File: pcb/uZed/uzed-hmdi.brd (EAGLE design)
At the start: 77.5 x 58.1 mm, 6 parts, among them U11 PCA9306

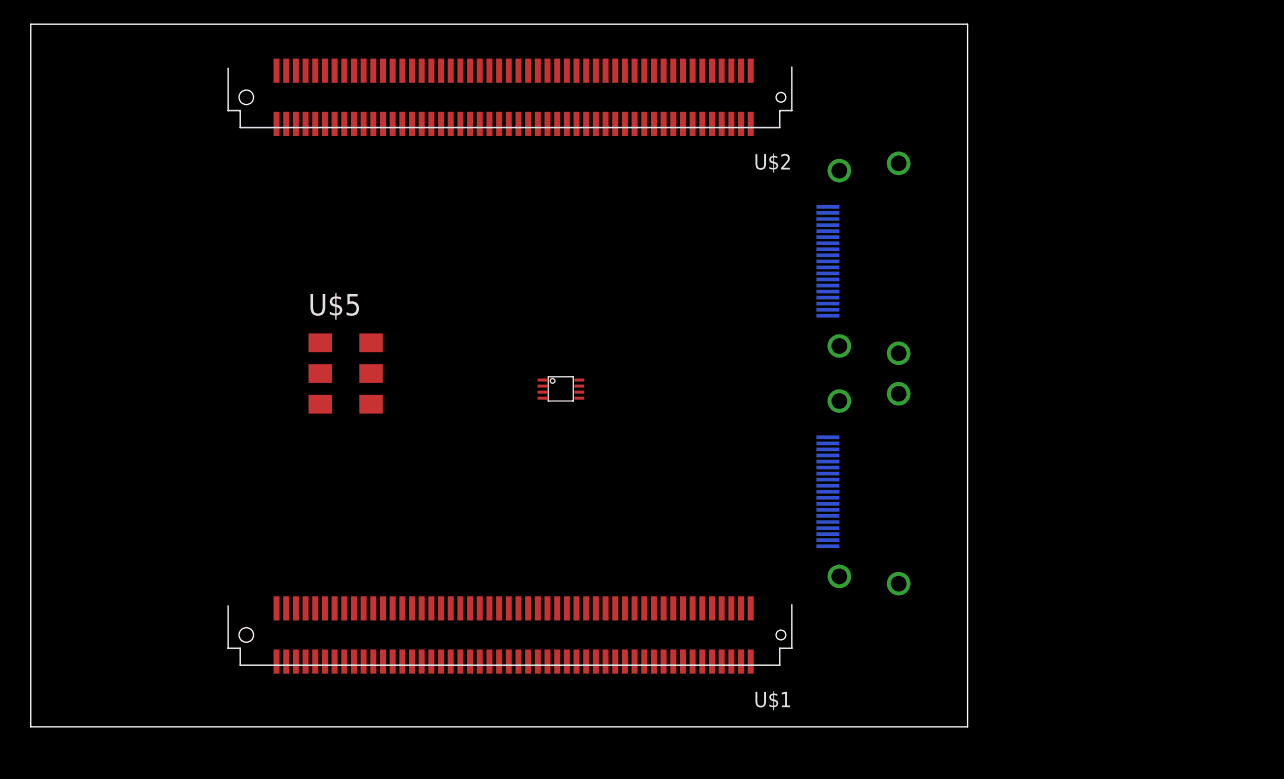
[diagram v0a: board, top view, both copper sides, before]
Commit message: hdmi connections copied in from scarab hardware board
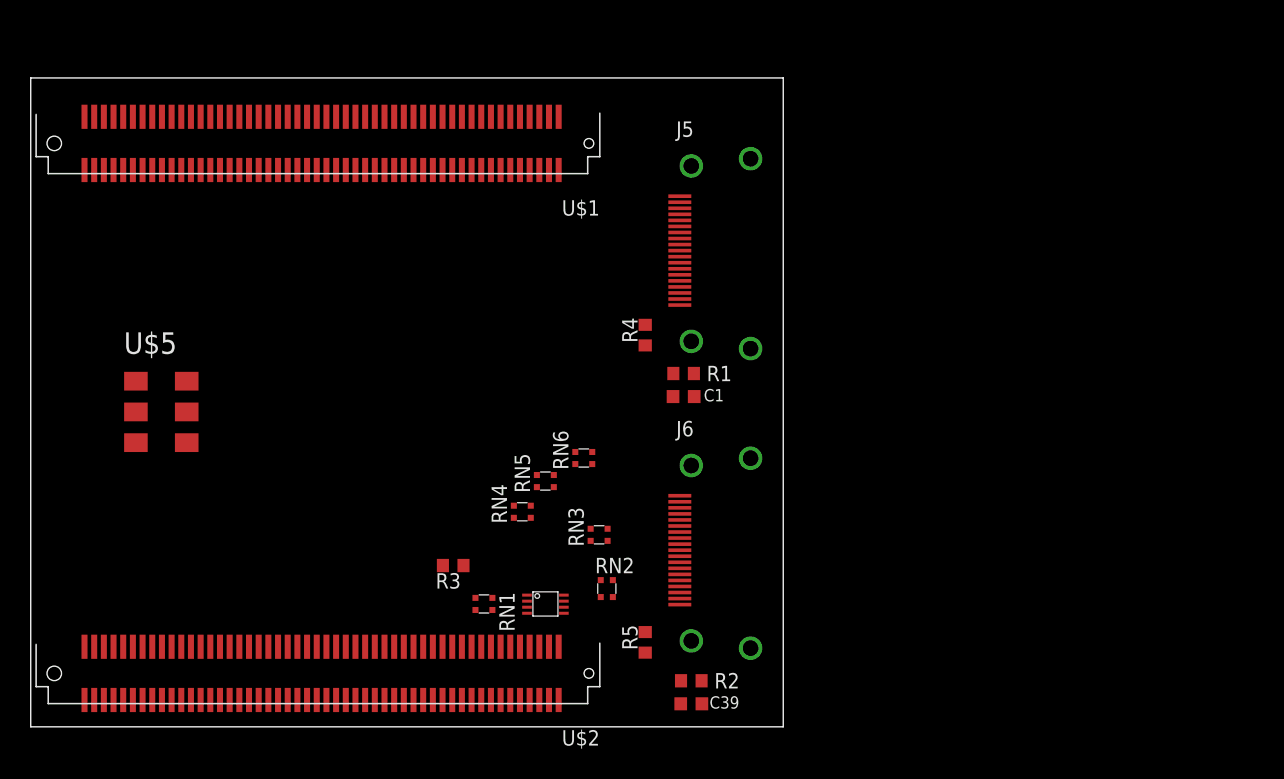
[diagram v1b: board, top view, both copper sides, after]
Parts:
- removed U$3, U$4: HDMI-A, new-connectors:HDMI_A
- removed U11: PCA9306, saanlima:PSOP-8
- added C1, C39: .1uF, rcl:C0603K
- added J5, J6: HDMI-TYPE-A-RECEPTICALFCI10029449, saanlima:FCI-HDMI-TYPE-A-RECEPT
- added PCA9306: PCA9306, saanlima:PSOP-8
- added R1, R2: 100K, rcl:R0603
- added R3: 0, rcl:R0603
- added R4, R5: 10K, rcl:R0603
- added RN1, RN2: 2k, resistor-dil:EXB34V
- added RN3, RN4, RN5, RN6: 51, resistor-dil:EXB34V
- moved U$2 50.2 mm to (4.45, 7.62)
- moved U$1 43.6 mm to (4.45, 51.4)
- moved U$5 15.6 mm to (10.8, 26.0)
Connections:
- new net 3V3: PCA9306.2, R3.2, RN1.3, RN1.4
- new net GND: C1.2, C39.2, J5.11, J5.14, J5.17, J5.2, J5.5, J5.8, J6.11, J6.14, J6.17, J6.2, J6.5, J6.8, PCA9306.1, R1.1, R2.1, R4.1
- new net N$1: C1.1, J5.SH1, J5.SH2, J5.SH3, J5.SH4, R1.2
- new net N$10: J5.19, R4.2
- new net N$11: R3.1, RN3.3, RN3.4, RN4.3, RN4.4, RN5.3, RN5.4, RN6.3, RN6.4
- new net N$12: J6.19, R5.1
- new net N$13: J6.18, PCA9306.7, PCA9306.8, R5.2, RN2.3, RN2.4
- new net N$15: J6.16, PCA9306.5, RN2.2
- new net N$16: J6.15, PCA9306.6, RN2.1
- new net N$17: PCA9306.3, RN1.1
- new net N$18: PCA9306.4, RN1.2
- new net N$19: J5.1
- new net N$2: J6.1, RN6.2
- new net N$20: J5.3
- new net N$21: J5.4
- new net N$22: J5.6
- new net N$23: J5.7
- new net N$24: J5.9
- new net N$25: J5.10
- new net N$26: J5.12
- new net N$3: J6.3, RN6.1
- new net N$34: C39.1, J6.SH1, J6.SH2, J6.SH3, J6.SH4, R2.2
- new net N$4: J6.4, RN5.2
- new net N$5: J6.6, RN5.1
- new net N$6: J6.7, RN4.2
- new net N$7: J6.9, RN4.1
- new net N$8: J6.10, RN3.2
- new net N$9: J6.12, RN3.1
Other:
- board size 77.5 x 58.1 mm -> 62.2 x 53.6 mm

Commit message: hdmi added in from scarab board
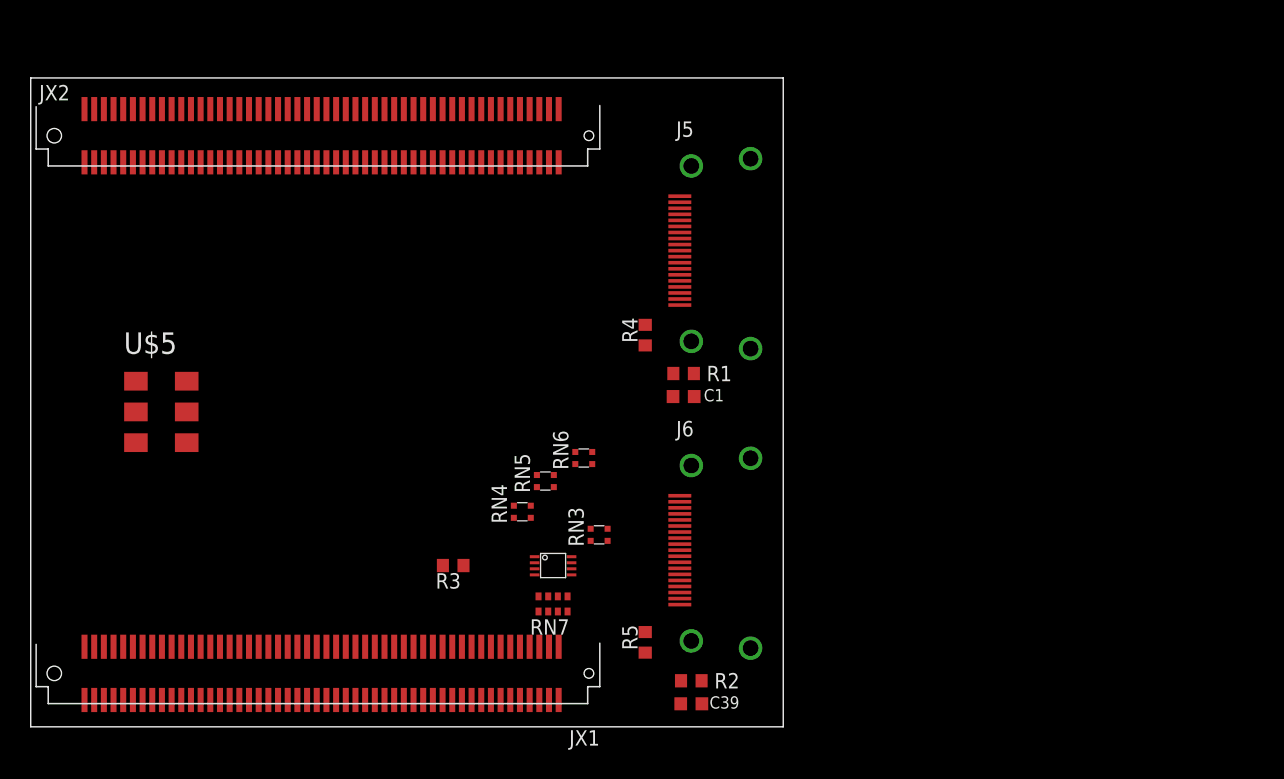
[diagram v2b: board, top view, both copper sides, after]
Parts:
- removed RN1, RN2: 2k, resistor-dil:EXB34V
- removed U$1: BERGSTAK-100POS, lupa300-components:BERG100POS
- added JX2: BERGSTAK-100POS, lupa300-components:BERG100POS
- added RN7: 2k, resistor-dil:0603-ARV
- moved PCA9306 3.24 mm to (43.2, 13.3)
- renumbered U$2 to JX1
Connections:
- net 3V3: now also RN7.1, RN7.2; no longer RN1.3, RN1.4
- net N$13: now also RN7.3, RN7.4; no longer RN2.3, RN2.4
- net N$15: now also RN7.6; no longer RN2.2
- net N$16: now also RN7.5; no longer RN2.1
- net N$17: now also RN7.7; no longer RN1.1
- net N$18: now also RN7.8; no longer RN1.2
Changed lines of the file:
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@@
 <dimension x1="0" y1="0" x2="62.21" y2="0" x3="31.105" y3="-5.08" textsize="1.778" layer="1"/>
 <dimension x1="0" y1="0" x2="0" y2="53.645" x3="-17.78" y3="26.8225" textsize="1.778" layer="1"/>
+<dimension x1="1.905" y1="4.445" x2="1.905" y2="48.895" x3="-9.525" y3="26.67" textsize="1.778" layer="1" unit="mil"/>
 </plain>
 <attributes>
@@
 </autorouter>
 <elements>
-<element name="U$1" library="lupa300-components" package="BERG100POS" value="BERGSTAK-100POS" x="4.445" y="51.435" smashed="yes" rot="R180">
-<attribute name="NAME" x="47.045" y="43.535" size="1.27" layer="25" rot="R180"/>
-</element>
-<element name="U$2" library="lupa300-components" package="BERG100POS" value="BERGSTAK-100POS" x="4.445" y="7.62" smashed="yes" rot="R180">
+<element name="JX2" library="lupa300-components" package="BERG100POS" value="BERGSTAK-100POS" x="4.445" y="52.07" smashed="yes" rot="R180">
+<attribute name="NAME" x="3.23" y="53.06" size="1.27" layer="25" rot="R180"/>
+</element>
+<element name="JX1" library="lupa300-components" package="BERG100POS" value="BERGSTAK-100POS" x="4.445" y="7.62" smashed="yes" rot="R180">
 <attribute name="NAME" x="47.045" y="-0.28" size="1.27" layer="25" rot="R180"/>
 </element>
@@
 <element name="R4" library="rcl" package="R0603" value="10K" x="50.8" y="32.385" rot="R90"/>
 <element name="R5" library="rcl" package="R0603" value="10K" x="50.8" y="6.985" rot="R90"/>
-<element name="PCA9306" library="saanlima" package="PSOP-8" value="PCA9306" x="42.545" y="10.16" rot="R270"/>
-<element name="RN1" library="resistor-dil" library_urn="urn:adsk.eagle:library:342" package="EXB34V" package3d_urn="urn:adsk.eagle:package:24930/1" value="2k" x="37.465" y="10.16" rot="R270">
-<attribute name="MF" value="" x="37.465" y="10.16" size="1.778" layer="27" rot="R270" display="off"/>
-<attribute name="MPN" value="" x="37.465" y="10.16" size="1.778" layer="27" rot="R270" display="off"/>
-<attribute name="OC_FARNELL" value="unknown" x="37.465" y="10.16" size="1.778" layer="27" rot="R270" display="off"/>
-<attribute name="OC_NEWARK" value="unknown" x="37.465" y="10.16" size="1.778" layer="27" rot="R270" display="off"/>
-</element>
-<element name="RN2" library="resistor-dil" library_urn="urn:adsk.eagle:library:342" package="EXB34V" package3d_urn="urn:adsk.eagle:package:24930/1" value="2k" x="47.625" y="11.43">
-<attribute name="MF" value="" x="47.625" y="11.43" size="1.778" layer="27" display="off"/>
-<attribute name="MPN" value="" x="47.625" y="11.43" size="1.778" layer="27" display="off"/>
-<attribute name="OC_FARNELL" value="unknown" x="47.625" y="11.43" size="1.778" layer="27" display="off"/>
-<attribute name="OC_NEWARK" value="unknown" x="47.625" y="11.43" size="1.778" layer="27" display="off"/>
+<element name="PCA9306" library="saanlima" package="PSOP-8" value="PCA9306" x="43.18" y="13.335" rot="R270"/>
+<element name="RN7" library="resistor-dil" package="0603-ARV" value="2k" x="43.18" y="10.16">
+<attribute name="MF" value="" x="43.18" y="10.16" size="1.778" layer="27" display="off"/>
+<attribute name="MPN" value="" x="43.18" y="10.16" size="1.778" layer="27" display="off"/>
+<attribute name="OC_FARNELL" value="unknown" x="43.18" y="10.16" size="1.778" layer="27" display="off"/>
+<attribute name="OC_NEWARK" value="unknown" x="43.18" y="10.16" size="1.778" layer="27" display="off"/>
 </element>
 </elements>
@@
 <wire x1="53.76" y1="3.81" x2="53.66" y2="11.105" width="0" layer="19" extent="1-1"/>
 <wire x1="53.735" y1="1.905" x2="53.76" y2="3.81" width="0" layer="19" extent="1-1"/>
-<wire x1="41.025" y1="10.89" x2="53.66" y2="11.105" width="0" layer="19" extent="1-1"/>
+<wire x1="41.66" y1="14.065" x2="53.66" y2="11.105" width="0" layer="19" extent="1-1"/>
 </signal>
 <signal name="N$34">
@@
 <contactref element="R3" pad="2"/>
 <contactref element="PCA9306" pad="2"/>
-<contactref element="RN1" pad="4"/>
-<contactref element="RN1" pad="3"/>
-<wire x1="38.165" y1="10.66" x2="41.025" y2="10.39" width="0" layer="19" extent="1-1"/>
-<wire x1="38.165" y1="9.66" x2="38.165" y2="10.66" width="0" layer="19" extent="1-1"/>
-<wire x1="34.075" y1="13.335" x2="38.165" y2="10.66" width="0" layer="19" extent="1-1"/>
+<contactref element="RN7" pad="2"/>
+<contactref element="RN7" pad="1"/>
+<wire x1="34.075" y1="13.335" x2="41.66" y2="13.565" width="0" layer="19" extent="1-1"/>
+<wire x1="42.78" y1="9.535" x2="34.075" y2="13.335" width="0" layer="19" extent="1-1"/>
+<wire x1="41.98" y1="9.535" x2="42.78" y2="9.535" width="0" layer="19" extent="1-1"/>
 </signal>
 <signal name="N$10">
@@
 <contactref element="PCA9306" pad="8"/>
 <contactref element="PCA9306" pad="7"/>
-<contactref element="RN2" pad="4"/>
-<contactref element="RN2" pad="3"/>
+<contactref element="RN7" pad="4"/>
+<contactref element="RN7" pad="3"/>
 <wire x1="50.8" y1="7.835" x2="53.66" y2="10.605" width="0" layer="19" extent="1-1"/>
-<wire x1="48.125" y1="12.13" x2="50.8" y2="7.835" width="0" layer="19" extent="1-1"/>
-<wire x1="47.125" y1="12.13" x2="48.125" y2="12.13" width="0" layer="19" extent="1-1"/>
-<wire x1="44.075" y1="10.89" x2="47.125" y2="12.13" width="0" layer="19" extent="1-1"/>
-<wire x1="44.075" y1="10.39" x2="44.075" y2="10.89" width="0" layer="19" extent="1-1"/>
+<wire x1="44.71" y1="13.565" x2="50.8" y2="7.835" width="0" layer="19" extent="1-1"/>
+<wire x1="44.71" y1="14.065" x2="44.71" y2="13.565" width="0" layer="19" extent="1-1"/>
+<wire x1="44.38" y1="9.535" x2="44.71" y2="14.065" width="0" layer="19" extent="1-1"/>
+<wire x1="43.58" y1="9.535" x2="44.38" y2="9.535" width="0" layer="19" extent="1-1"/>
 </signal>
 <signal name="N$15">
 <contactref element="J6" pad="16"/>
 <contactref element="PCA9306" pad="5"/>
-<contactref element="RN2" pad="2"/>
-<wire x1="48.125" y1="10.73" x2="53.66" y2="11.605" width="0" layer="19" extent="1-1"/>
-<wire x1="44.075" y1="9.39" x2="48.125" y2="10.73" width="0" layer="19" extent="1-1"/>
+<contactref element="RN7" pad="6"/>
+<wire x1="44.71" y1="12.565" x2="53.66" y2="11.605" width="0" layer="19" extent="1-1"/>
+<wire x1="43.58" y1="10.785" x2="44.71" y2="12.565" width="0" layer="19" extent="1-1"/>
 </signal>
 <signal name="N$16">
 <contactref element="J6" pad="15"/>
 <contactref element="PCA9306" pad="6"/>
-<contactref element="RN2" pad="1"/>
-<wire x1="47.125" y1="10.73" x2="53.66" y2="12.105" width="0" layer="19" extent="1-1"/>
-<wire x1="44.075" y1="9.89" x2="47.125" y2="10.73" width="0" layer="19" extent="1-1"/>
+<contactref element="RN7" pad="5"/>
+<wire x1="44.71" y1="13.065" x2="53.66" y2="12.105" width="0" layer="19" extent="1-1"/>
+<wire x1="44.38" y1="10.785" x2="44.71" y2="13.065" width="0" layer="19" extent="1-1"/>
 </signal>
 <signal name="N$17">
 <contactref element="PCA9306" pad="3"/>
-<contactref element="RN1" pad="1"/>
-<wire x1="36.765" y1="10.66" x2="41.025" y2="9.89" width="0" layer="19" extent="1-1"/>
+<contactref element="RN7" pad="7"/>
+<wire x1="42.78" y1="10.785" x2="41.66" y2="13.065" width="0" layer="19" extent="1-1"/>
 </signal>
 <signal name="N$18">
 <contactref element="PCA9306" pad="4"/>
-<contactref element="RN1" pad="2"/>
-<wire x1="36.765" y1="9.66" x2="41.025" y2="9.39" width="0" layer="19" extent="1-1"/>
+<contactref element="RN7" pad="8"/>
+<wire x1="41.98" y1="10.785" x2="41.66" y2="12.565" width="0" layer="19" extent="1-1"/>
 </signal>
 <signal name="N$19">

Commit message: more work on hdmi, layout with mounting holes complete, bergstak connectors aligned to be to carrier board spec
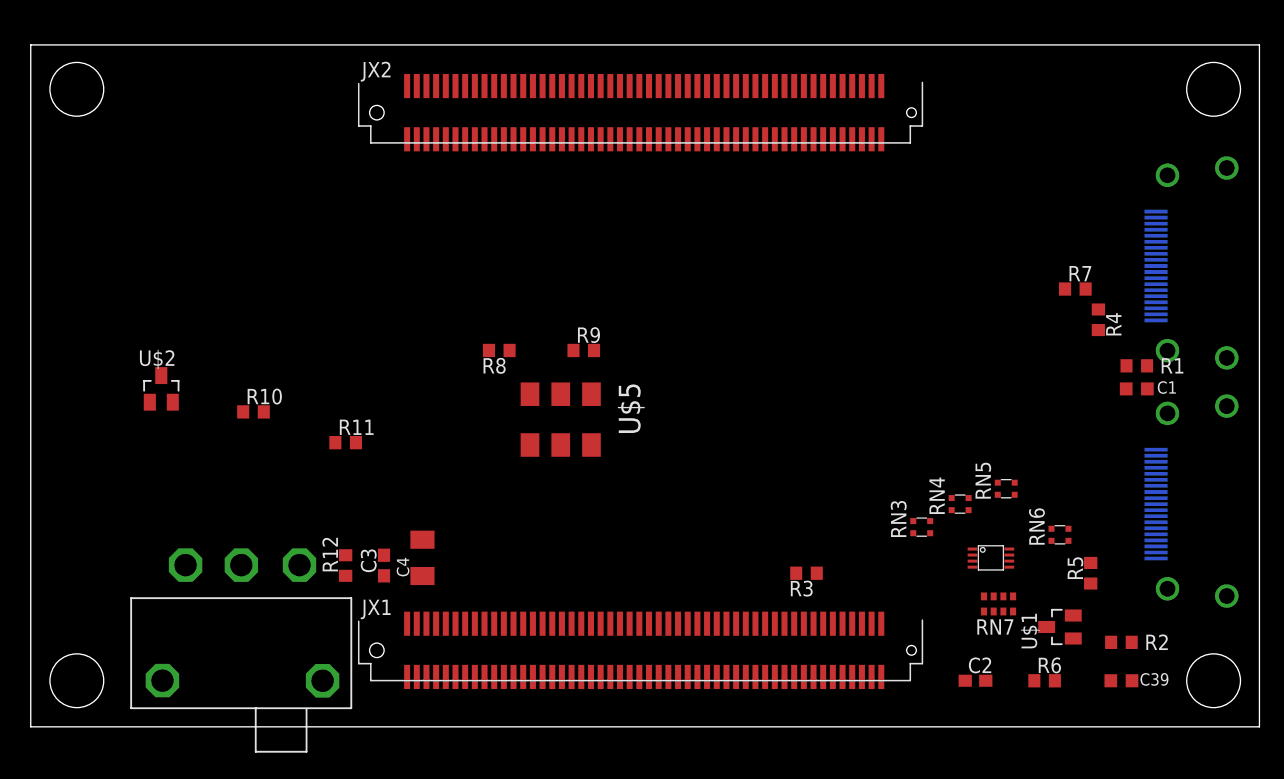
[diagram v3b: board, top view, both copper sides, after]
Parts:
- added C2: 100nF, rcl:C0603
- added C3: (no value), rcl:C0603
- added C4: (no value), rcl:C1206K
- added POWER_SW: T511006, lupa300-components:SPDT
- added R10, R8, R9: 2k2, rcl:R0603
- added R11: 3k92, rcl:R0603
- added R12: DNP, rcl:R0603
- added R6: 10K, rcl:R0603
- added R7: 0, rcl:R0603
- added U$1, U$2: BSS138, lupa300-components:SOT23
- moved RN6 39.9 mm to (85.1, 15.9)
- moved J6 39.6 mm to (94.0, 18.4), flipped to the bottom, turned to 180 degrees
- moved J5 39.4 mm to (94.0, 38.1), flipped to the bottom, turned to 180 degrees
- moved RN5 38.1 mm to (80.6, 19.7)
- moved R4 37.5 mm to (88.3, 33.7), turned to 270 degrees
- moved C1 37.5 mm to (91.4, 27.9)
- moved R1 37.5 mm to (91.4, 29.8)
- moved R5 37.3 mm to (87.6, 12.7)
- moved RN7 36.8 mm to (80.0, 10.2)
- moved PCA9306 36.2 mm to (79.4, 14.0)
- moved RN4 36.2 mm to (76.8, 18.4)
- moved R2 35.7 mm to (90.2, 6.99)
- moved C39 35.6 mm to (90.2, 3.81)
- moved U$5 33.0 mm to (43.8, 25.4), turned to 270 degrees
- moved R3 29.2 mm to (64.1, 12.7)
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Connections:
- net N$17 renamed SCL2
- net N$18 renamed SDA2
- net N$19 renamed P2_DATA2+
- net N$2 renamed P1_DATA2+
- net N$20 renamed P2_DATA2-
- net N$21 renamed P2_DATA1+
- net N$22 renamed P2_DATA1-
- net N$23 renamed P2_DATA0+
- net N$24 renamed P2_DATA0-
- net N$25 renamed P2_CLOCK+
- net N$26 renamed P2_CLOCK-
- net N$3 renamed P1_DATA2-
- net N$4 renamed P1_DATA1+
- net N$5 renamed P1_DATA1-
- net N$6 renamed P1_DATA0+
- net N$7 renamed P1_DATA0-
- net N$8 renamed P1_CLOCK+
- net N$9 renamed P1_CLOCK-
- removed net N$13: J6.18, PCA9306.7, PCA9306.8, R5.2, RN7.3, RN7.4
- new net 3.3V: R8.2, R9.2
- new net 5V: C3.1, C4.1, J6.18, JX1.P$41, JX1.P$42, JX1.P$43, JX1.P$44, JX2.P$41, JX2.P$42, JX2.P$43, JX2.P$44, PCA9306.7, PCA9306.8, POWER_SW.P$3, R12.1, R5.2, R7.1, RN7.3, RN7.4
- new net 5V_OFF: POWER_SW.P$5
- new net DET_CONTROL: R6.2, U$1.1
- new net HDMI_CLOCK: JX1.P$60, U$5.P$4
- new net N$14: J5.18, R7.2
- new net N$2: R11.2, U$2.1
- new net PGOOD_CARRIER: JX2.P$90
- new net PWR_EN: JX1.P$96
- new net SDA1: R8.1, U$5.P$1
- new net SDL1: R9.1, U$5.P$2
- new net VCCIO_EN: JX2.P$91
- new net VIN: POWER_SW.P$4, R12.2
- net 3V3: now also C2.1, JX1.P$21, JX1.P$22, JX1.P$23, JX1.P$24, JX2.P$21, JX2.P$22, JX2.P$23, JX2.P$24, R6.1, U$5.P$6
- net GND: now also C2.2, C3.2, C4.2, JX1.P$1, JX1.P$15, JX1.P$16, JX1.P$2, JX1.P$29, JX1.P$3, JX1.P$30, JX1.P$35, JX1.P$36, JX1.P$4, JX1.P$49, JX1.P$5, JX1.P$50, JX1.P$55, JX1.P$56, JX1.P$6, JX1.P$61, JX1.P$62, JX1.P$67, JX1.P$68, JX1.P$73, JX1.P$74, JX1.P$79, JX1.P$80, JX1.P$85, JX1.P$86, JX2.P$10, JX2.P$15, JX2.P$16, JX2.P$29, JX2.P$30, JX2.P$35, JX2.P$36, JX2.P$49, JX2.P$50, JX2.P$55, JX2.P$56, JX2.P$61, JX2.P$62, JX2.P$67, JX2.P$68, JX2.P$73, JX2.P$74, JX2.P$79, JX2.P$80, JX2.P$85, JX2.P$86, JX2.P$9, U$1.2, U$5.P$3
- net N$12: now also U$1.3
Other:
- board size 62.2 x 53.6 mm -> 101.6 x 56.4 mm
